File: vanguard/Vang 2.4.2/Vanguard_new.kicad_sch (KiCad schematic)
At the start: 87 parts, among them J1 USB_C_Receptacle_USB2.0_16P, J2 Micro_SD_Card_Det1, J3 Conn_02x03_Odd_Even, J4 Conn_01x03, J5 Conn_01x03, J6 Conn_01x03, J7 Conn_01x02_Pin, Q1 BSS138, Q2 BSS138, Q3 BSS138, Q4 BSS138, U1 TXB0104D, U10 AP2112K-3.3, U2 TPS82130SILR, U3 ATSAMD11D14A-M, U4 BMP390L, U5 BD1020HFV-TR, U6 AT25DF641A-SH-T, U7 ATmega4809-A, U8 BNO055, U9 TPS61092, Y1 Crystal

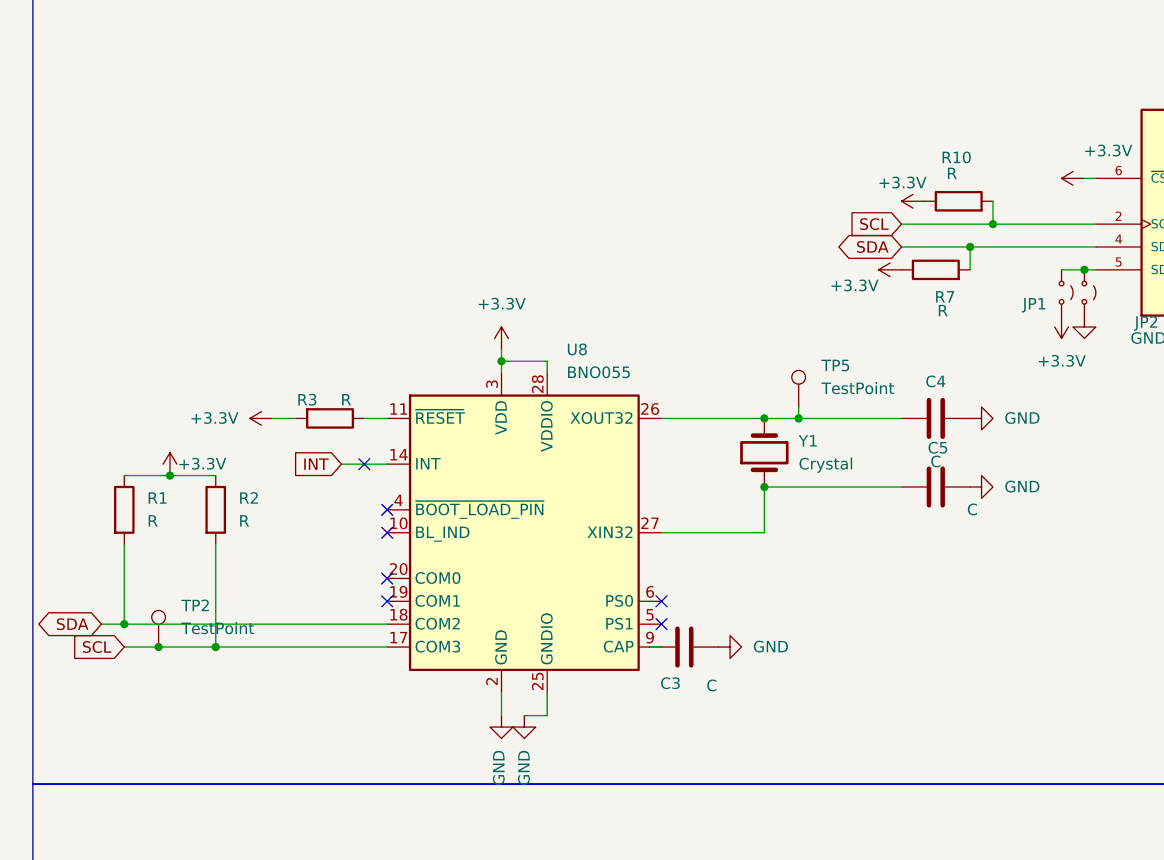
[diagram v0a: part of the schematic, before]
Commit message: sensor - r and c values + a testpoint at boot pin
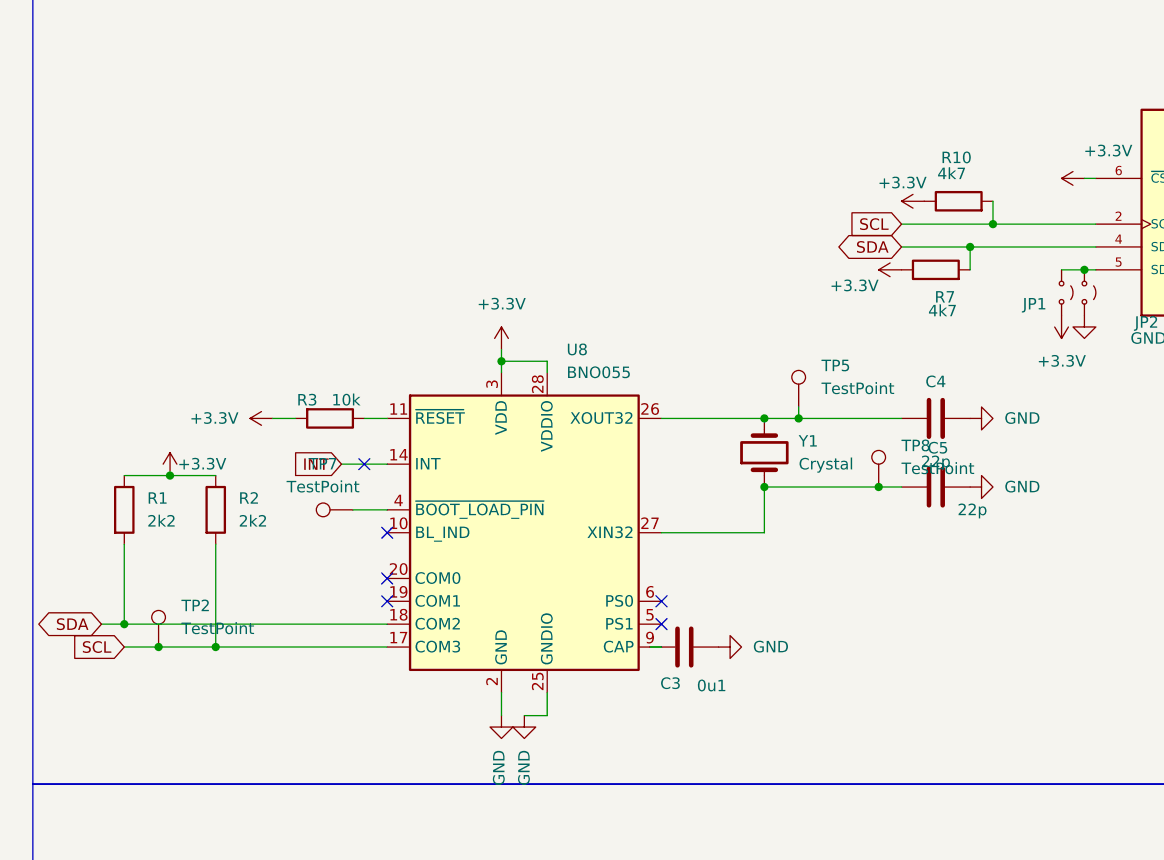
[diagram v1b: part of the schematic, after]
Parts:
- added TP7: TestPoint, symbol Connector:TestPoint
- added TP8: TestPoint, TestPoint:TestPoint_Pad_1.0x1.0mm, symbol Connector:TestPoint
- C3: value C -> 0u1
- C4, C5: value C -> 22p
- R1, R2: value R -> 2k2
- R10, R7: value R -> 4k7
- R3: value R -> 10k
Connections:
- net at C5.1, U8.27 (XIN32), Y1.1: now also TP8.1
- net at U8.4 (~{BOOT_LOAD_PIN}): now also TP7.1
- no-connect marks 43 -> 42
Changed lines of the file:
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@@
 	)
 	(junction
+		(at 106.68 160.02)
+		(diameter 0)
+		(color 0 0 0 0)
+	)
+	(junction
 		(at 97.79 152.4)
 		(diameter 0)
@@
 	)
 	(no_connect
-		(at 52.07 162.56)
-	)
-	(no_connect
 		(at 43.18 52.07)
 	)
@@
 	(wire
 		(pts
+			(xy 48.26 162.56) (xy 52.07 162.56)
+		)
+		(stroke
+			(width 0)
+			(type default)
+		)
+	)
+	(wire
+		(pts
 			(xy 171.45 43.18) (xy 175.26 43.18)
 		)
@@
 	(wire
 		(pts
-			(xy 93.98 160.02) (xy 109.22 160.02)
+			(xy 93.98 160.02) (xy 106.68 160.02)
 		)
 		(stroke
@@
 	(wire
 		(pts
+			(xy 106.68 160.02) (xy 109.22 160.02)
+		)
+		(stroke
+			(width 0)
+			(type default)
+		)
+	)
+	(wire
+		(pts
 			(xy 353.06 48.26) (xy 353.06 50.8)
 		)
@@
 			)
 		)
-		(property "Value" "R"
+		(property "Value" "4k7"
 			(at 114.808 125.222 90)
 			(effects
@@
 	)
 	(symbol
+		(lib_id "Connector:TestPoint")
+		(at 48.26 162.56 90)
+		(unit 1)
+		(exclude_from_sim no)
+		(in_bom yes)
+		(on_board yes)
+		(dnp no)
+		(fields_autoplaced yes)
+		(property "Reference" "TP7"
+			(at 44.958 157.48 90)
+			(effects
+				(font
+					(size 1.27 1.27)
+				)
+			)
+		)
+		(property "Value" "TestPoint"
+			(at 44.958 160.02 90)
+			(effects
+				(font
+					(size 1.27 1.27)
+				)
+			)
+		)
+		(property "Footprint" ""
+			(at 48.26 157.48 0)
+			(effects
+				(font
+					(size 1.27 1.27)
+				)
+				(hide yes)
+			)
+		)
+		(property "Datasheet" "~"
+			(at 48.26 157.48 0)
+			(effects
+				(font
+					(size 1.27 1.27)
+				)
+				(hide yes)
+			)
+		)
+		(property "Description" "test point"
+			(at 48.26 162.56 0)
+			(effects
+				(font
+					(size 1.27 1.27)
+				)
+				(hide yes)
+			)
+		)
+		(pin "1"
+		)
+		(instances
+			(project ""
+				(path "/972fbf12-2dcd-4fdf-b1c9-8a2880c46640"
+					(reference "TP7")
+					(unit 1)
+				)
+			)
+		)
+	)
+	(symbol
 		(lib_id "power:+3.3V")
 		(at 170.18 120.65 270)
@@
 			)
 		)
-		(property "Value" "R"
+		(property "Value" "10k"
 			(at 47.498 150.368 90)
 			(effects
@@
 			)
 		)
-		(property "Value" "C"
+		(property "Value" "22p"
 			(at 117.094 162.56 90)
 			(effects
@@
 			)
 		)
-		(property "Value" "R"
+		(property "Value" "2k2"
 			(at 35.56 163.8299 0)
 			(effects
@@
 			)
 		)
-		(property "Value" "C"
+		(property "Value" "0u1"
 			(at 88.138 182.118 90)
 			(effects
@@
 			)
 		)
-		(property "Value" "C"
+		(property "Value" "22p"
 			(at 113.03 157.226 90)
 			(effects
@@
 	)
 	(symbol
+		(lib_id "Connector:TestPoint")
+		(at 106.68 160.02 0)
+		(unit 1)
+		(exclude_from_sim no)
+		(in_bom yes)
+		(on_board yes)
+		(dnp no)
+		(fields_autoplaced yes)
+		(property "Reference" "TP8"
+			(at 109.22 155.4479 0)
+			(effects
+				(font
+					(size 1.27 1.27)
+				)
+				(justify left)
+			)
+		)
+		(property "Value" "TestPoint"
+			(at 109.22 157.9879 0)
+			(effects
+				(font
+					(size 1.27 1.27)
+				)
+				(justify left)
+			)
+		)
+		(property "Footprint" "TestPoint:TestPoint_Pad_1.0x1.0mm"
+			(at 111.76 160.02 0)
+			(effects
+				(font
+					(size 1.27 1.27)
+				)
+				(hide yes)
+			)
+		)
+		(property "Datasheet" "~"
+			(at 111.76 160.02 0)
+			(effects
+				(font
+					(size 1.27 1.27)
+				)
+				(hide yes)
+			)
+		)
+		(property "Description" "test point"
+			(at 106.68 160.02 0)
+			(effects
+				(font
+					(size 1.27 1.27)
+				)
+				(hide yes)
+			)
+		)
+		(pin "1"
+		)
+		(instances
+			(project "Vanguard_new"
+				(path "/972fbf12-2dcd-4fdf-b1c9-8a2880c46640"
+					(reference "TP8")
+					(unit 1)
+				)
+			)
+		)
+	)
+	(symbol
 		(lib_id "Device:R")
 		(at 22.86 162.56 0)
@@
 			)
 		)
-		(property "Value" "R"
+		(property "Value" "2k2"
 			(at 25.4 163.8299 0)
 			(effects
@@
 			)
 		)
-		(property "Value" "R"
+		(property "Value" "4k7"
 			(at 113.792 140.462 90)
 			(effects

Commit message: servo power r&c
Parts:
- C12: value C -> 2u2
- C13: value C_Polarized_US -> 100u
- C8: value C -> 10u
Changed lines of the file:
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@@
 			)
 		)
-		(property "Value" "C"
+		(property "Value" "10u"
 			(at 348.742 172.72 0)
 			(effects
@@
 			)
 		)
-		(property "Value" "C_Polarized_US"
+		(property "Value" "100u"
 			(at 409.702 162.306 0)
 			(effects
@@
 			)
 		)
-		(property "Value" "C"
+		(property "Value" "2u2"
 			(at 400.05 162.56 0)
 			(effects

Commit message: usb c footpinrt
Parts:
- J1: footprint Connector_USB:USB-C-SMD_JLC REPLACEMENT -> Connector_USB:USB_C_Receptacle_Amphenol_124019772112A
- TP7: footprint (none) -> TestPoint:TestPoint_Pad_1.0x1.0mm
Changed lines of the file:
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@@
 			)
 		)
-		(property "Footprint" ""
+		(property "Footprint" "TestPoint:TestPoint_Pad_1.0x1.0mm"
 			(at 48.26 157.48 0)
 			(effects
@@
 			)
 		)
-		(property "Footprint" "Connector_USB:USB-C-SMD_JLC REPLACEMENT"
+		(property "Footprint" "Connector_USB:USB_C_Receptacle_Amphenol_124019772112A"
 			(at 31.75 39.37 0)
 			(effects

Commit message: the inductor footprint assigned
Thank GOD!!! hoho! after 34 hours!
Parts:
- L1: footprint SLF7055T-6R8N2R8-3PF:IND_SLF7055T-6R8N2R8-3PF -> inductor:IND_SLF7055T-6R8N2R8-3PF.kicad_mod
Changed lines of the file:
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@@
 			)
 		)
-		(property "Footprint" "SLF7055T-6R8N2R8-3PF:IND_SLF7055T-6R8N2R8-3PF"
+		(property "Footprint" "inductor:IND_SLF7055T-6R8N2R8-3PF.kicad_mod"
 			(at 356.87 157.48 0)
 			(effects

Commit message: buzzer footprint assigned!
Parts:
- LS1: footprint KXG1203C:XDCR_KXG1203C -> buzzer:XDCR_KXG1203C.kicad_mod
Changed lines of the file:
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@@
 			)
 		)
-		(property "Footprint" "KXG1203C:XDCR_KXG1203C"
+		(property "Footprint" "buzzer:XDCR_KXG1203C.kicad_mod"
 			(at 407.67 107.95 0)
 			(effects

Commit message: assigned barometer footprint
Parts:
- U2: footprint TPS82130SILR:CONV_TPS82140SILR -> buck_convertor:CONV_TPS82140SILR.kicad_mod
- U4: footprint BMP390L:XDCR_BMP390L -> barometer:XDCR_BMP390L.kicad_mod
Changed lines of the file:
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@@
 			)
 		)
-		(property "Footprint" "BMP390L:XDCR_BMP390L"
+		(property "Footprint" "barometer:XDCR_BMP390L.kicad_mod"
 			(at 151.13 130.81 0)
 			(effects
@@
 			)
 		)
-		(property "Footprint" "TPS82130SILR:CONV_TPS82140SILR"
+		(property "Footprint" "buck_convertor:CONV_TPS82140SILR.kicad_mod"
 			(at 326.39 43.18 0)
 			(effects

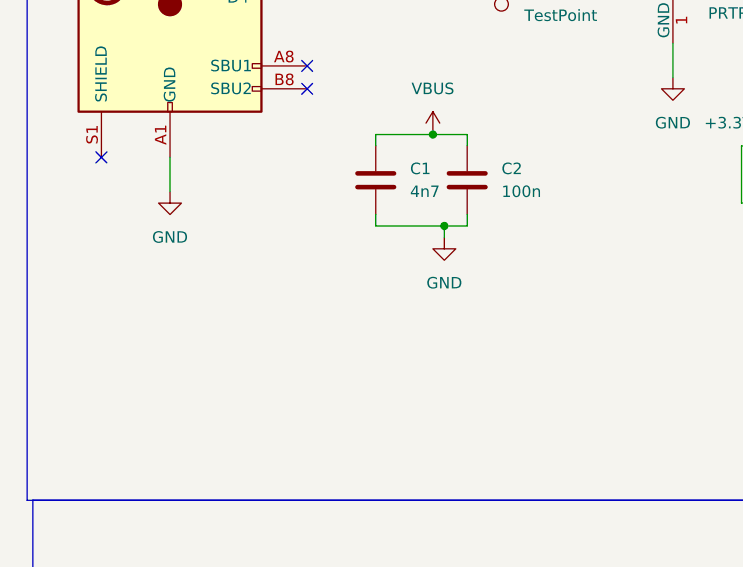
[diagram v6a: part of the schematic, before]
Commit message: added button switch
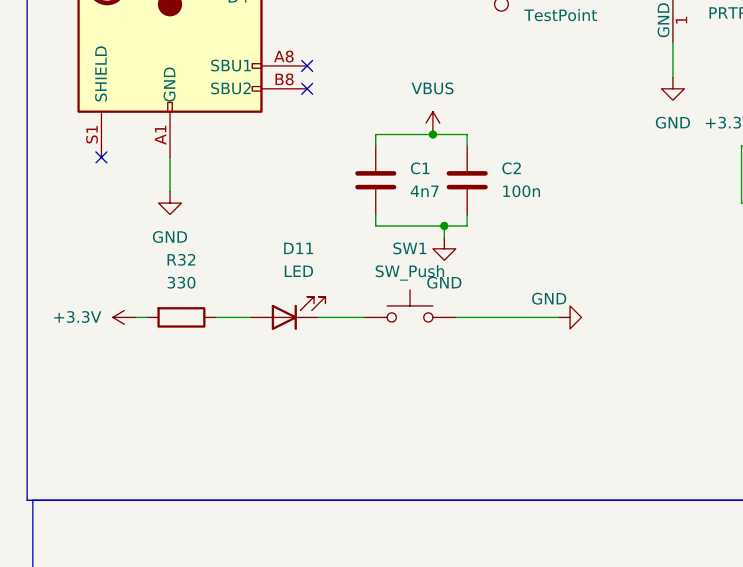
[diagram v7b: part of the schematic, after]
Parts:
- added D11: LED, LED_SMD:LED_0201_0603Metric, symbol Device:LED
- added R32: 330, Resistor_SMD:R_0402_1005Metric, symbol Device:R
- added SW1: SW_Push, symbol Switch:SW_Push
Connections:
- net +3.3V: now also R32.2
- net GND: now also SW1.2
- new net: D11.1 (K), SW1.1
- new net: D11.2 (A), R32.1

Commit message: buzzer fix
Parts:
- removed LS1: KXG1203C, buzzer:XDCR_KXG1203C.kicad_mod, symbol KXG1203C[1]:KXG1203C
- added BZ1: Buzzer, Buzzer_Beeper:MagneticBuzzer_Kingstate_KCG0601, symbol Device:Buzzer
- added R34: 2k2, Resistor_SMD:R_0402_1005Metric, symbol Device:R
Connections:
- net +3.3V: now also BZ1.1 (+); no longer Q4.2 (S)
- net GND: now also Q4.2 (S), R34.2; no longer Q4.1 (G), U7.16 (PC4)
- net at Q4.3 (D): now also BZ1.2 (-)
- new net BUZZER: Q4.1 (G), R34.1, U7.16 (PC4)
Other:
- moved on the sheet: Q4
